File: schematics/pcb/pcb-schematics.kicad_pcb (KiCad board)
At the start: 2 copper layers, 145 x 77 mm, 0 parts

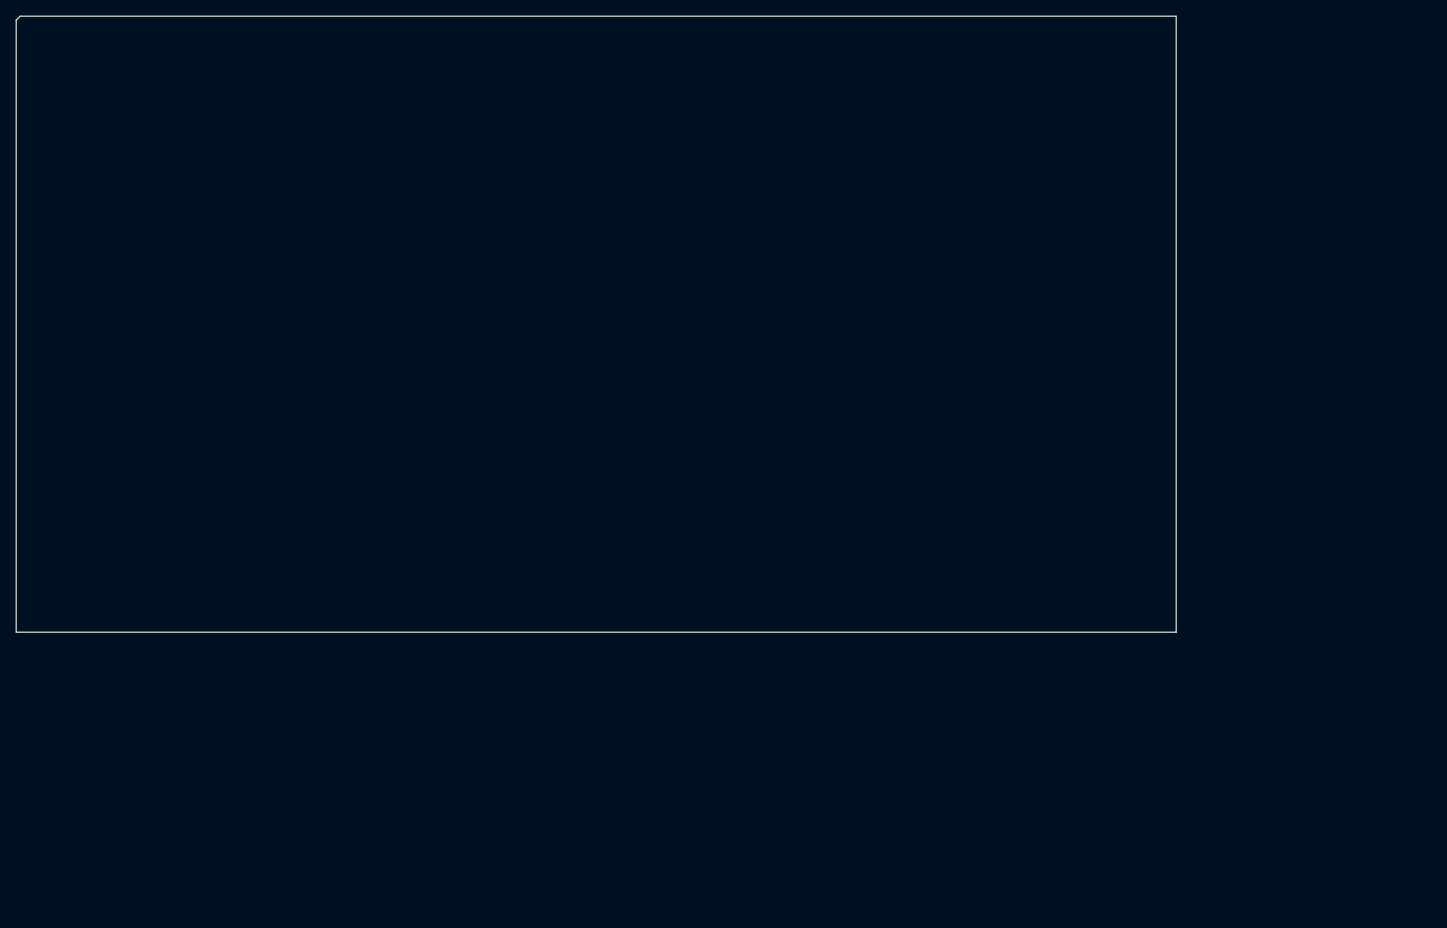
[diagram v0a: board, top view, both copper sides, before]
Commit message: schematic and driver rewrite
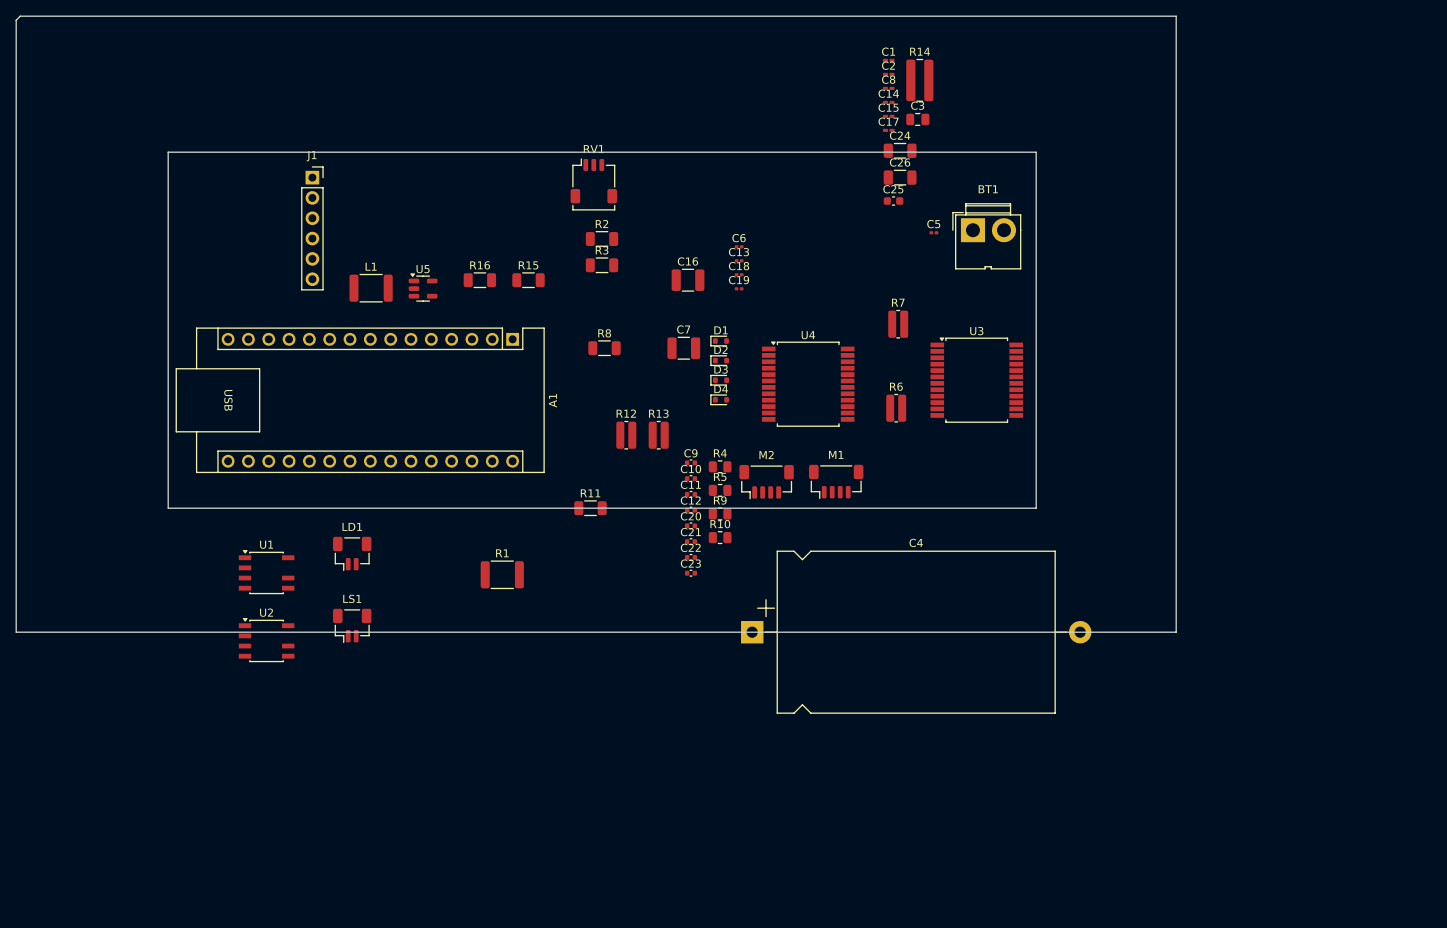
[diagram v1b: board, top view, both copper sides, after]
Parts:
- added A1: Arduino_Nano_33_BLE, Module:Arduino_Nano, F.Cu at (117.5, 88.4)
- added BT1: 9V, Connector:JWT_A3963_1x02_P3.96mm_Vertical, F.Cu at (175.1, 74.8)
- added C1: 10uF, Capacitor_SMD:C_0201_0603Metric_Pad0.64x0.40mm_HandSolder, F.Cu at (164.6, 53.5)
- added C10: 1000pF, Capacitor_SMD:C_0402_1005Metric, F.Cu at (139.9, 105.8)
- added C11: 1000pF, Capacitor_SMD:C_0402_1005Metric, F.Cu at (139.9, 107.8)
- added C12: 0.068uF, Capacitor_SMD:C_0402_1005Metric, F.Cu at (139.9, 109.7)
- added C13: 0.1uF, Capacitor_SMD:C_0201_0603Metric, F.Cu at (145.9, 78.6)
- added C14: 10uF, Capacitor_SMD:C_0201_0603Metric_Pad0.64x0.40mm_HandSolder, F.Cu at (164.6, 58.8)
- added C15: 0.1uF, Capacitor_SMD:C_0201_0603Metric_Pad0.64x0.40mm_HandSolder, F.Cu at (164.6, 60.5)
- added C16: 100uF, Capacitor_SMD:C_1210_3225Metric, F.Cu at (139.5, 81.0)
- added C17: 0.1uF, Capacitor_SMD:C_0201_0603Metric_Pad0.64x0.40mm_HandSolder, F.Cu at (164.6, 62.3)
- added C18: 0.01uF, Capacitor_SMD:C_0201_0603Metric, F.Cu at (145.9, 80.3)
- added C19: 0.22uF, Capacitor_SMD:C_0201_0603Metric, F.Cu at (145.9, 82.1)
- added C2: 10uF, Capacitor_SMD:C_0201_0603Metric_Pad0.64x0.40mm_HandSolder, F.Cu at (164.6, 55.3)
- added C20: 0.068uF, Capacitor_SMD:C_0402_1005Metric, F.Cu at (139.9, 111.7)
- added C21: 5600pF, Capacitor_SMD:C_0402_1005Metric, F.Cu at (139.9, 113.7)
- added C22: 1000pF, Capacitor_SMD:C_0402_1005Metric, F.Cu at (139.9, 115.7)
- added C23: 1000pF, Capacitor_SMD:C_0402_1005Metric, F.Cu at (139.9, 117.6)
- added C24: 22uF, Capacitor_SMD:C_1206_3216Metric, F.Cu at (166.0, 64.8)
- added C25: 4.7uF, Capacitor_SMD:C_0603_1608Metric, F.Cu at (165.2, 71.1)
- added C26: 22uF, Capacitor_SMD:C_1206_3216Metric, F.Cu at (166.0, 68.2)
- added C3: 0.05uF, Capacitor_SMD:C_0805_2012Metric, F.Cu at (168.2, 60.9)
- added C4: 250uF, Capacitor_THT:CP_Axial_L34.5mm_D20.0mm_P41.00mm_Horizontal, F.Cu at (147.5, 125.0)
- added C5: 0.01uF, Capacitor_SMD:C_0201_0603Metric, F.Cu at (170.2, 75.1)
- added C6: 0.22uF, Capacitor_SMD:C_0201_0603Metric, F.Cu at (145.9, 76.8)
- added C7: 100uF, Capacitor_SMD:C_1210_3225Metric, F.Cu at (139.0, 89.5)
- added C8: 0.1uF, Capacitor_SMD:C_0201_0603Metric_Pad0.64x0.40mm_HandSolder, F.Cu at (164.6, 57.0)
- added C9: 5600pF, Capacitor_SMD:C_0402_1005Metric, F.Cu at (139.9, 103.8)
- added D1: 1N4148, Diode_SMD:D_SOD-523, F.Cu at (143.6, 88.6)
- added D2: 1N4148, Diode_SMD:D_SOD-523, F.Cu at (143.6, 91.1)
- added D3: 1N4148, Diode_SMD:D_SOD-523, F.Cu at (143.6, 93.5)
- added D4: 1N4148, Diode_SMD:D_SOD-523, F.Cu at (143.6, 96.0)
- added J1: Micro_SD_Card, Connector_PinSocket_2.54mm:PinSocket_1x06_P2.54mm_Vertical, F.Cu at (92.5, 68.2)
- added L1: 2.2uH, Inductor_SMD:L_1812_4532Metric, F.Cu at (99.9, 82.0)
- added LD1: D_Laser_1C2A, Connector_Molex:Molex_Pico-Clasp_501331-0207_1x02-1MP_P1.00mm_Vertical, F.Cu at (97.5, 115.2)
- added LS1: Speaker, Connector_Molex:Molex_Pico-Clasp_501331-0207_1x02-1MP_P1.00mm_Vertical, F.Cu at (97.5, 124.2)
- added M1: Stepper_Motor_bipolar, Connector_Molex:Molex_Pico-Clasp_501331-0407_1x04-1MP_P1.00mm_Vertical, F.Cu at (158.0, 106.2)
- added M2: Stepper_Motor_bipolar, Connector_Molex:Molex_Pico-Clasp_501331-0407_1x04-1MP_P1.00mm_Vertical, F.Cu at (149.3, 106.2)
- added R1: 10, Resistor_SMD:R_1812_4532Metric, F.Cu at (116.3, 117.8)
- added R10: 0.3, Resistor_SMD:R_0805_2012Metric, F.Cu at (143.5, 113.2)
- added R11: 100K, Resistor_SMD:R_1206_3216Metric, F.Cu at (127.3, 109.5)
- added R12: 39K, Resistor_SMD:R_0612_1632Metric, F.Cu at (131.8, 100.4)
- added R13: 39K, Resistor_SMD:R_0612_1632Metric, F.Cu at (135.8, 100.4)
- added R14: 1K, Resistor_SMD:R_1020_2550Metric, F.Cu at (168.4, 56.0)
- added R15: 200K, Resistor_SMD:R_1206_3216Metric, F.Cu at (119.5, 81.0)
- added R16: 100K, Resistor_SMD:R_1206_3216Metric, F.Cu at (113.5, 81.0)
- added R2: 100, Resistor_SMD:R_1206_3216Metric, F.Cu at (128.7, 75.8)
- added R3: 100K, Resistor_SMD:R_1206_3216Metric, F.Cu at (128.7, 79.1)
- added R4: 0.3, Resistor_SMD:R_0805_2012Metric, F.Cu at (143.5, 104.3)
- added R5: 0.3, Resistor_SMD:R_0805_2012Metric, F.Cu at (143.5, 107.3)
- added R6: 39K, Resistor_SMD:R_0612_1632Metric, F.Cu at (165.5, 97.0)
- added R7: 39K, Resistor_SMD:R_0612_1632Metric, F.Cu at (165.8, 86.5)
- added R8: 100, Resistor_SMD:R_1206_3216Metric, F.Cu at (129.0, 89.5)
- added R9: 0.3, Resistor_SMD:R_0805_2012Metric, F.Cu at (143.5, 110.2)
- added RV1: 10K, Connector_Molex:Molex_Pico-Clasp_202396-0307_1x03-1MP_P1.00mm_Horizontal, F.Cu at (127.7, 68.6)
- added U1: LM386, Package_SO:SOIC-8-N7_3.9x4.9mm_P1.27mm, F.Cu at (86.8, 117.6)
- added U2: MCP4901, Package_SO:SOIC-8-N7_3.9x4.9mm_P1.27mm, F.Cu at (86.8, 126.1)
- added U3: L6208D, Package_SO:ST_PowerSSO-24_SlugUp, F.Cu at (175.6, 93.5)
- added U4: L6208D, Package_SO:ST_PowerSSO-24_SlugUp, F.Cu at (154.5, 94.0)
- added U5: TLV62568DBV, Package_TO_SOT_SMD:SOT-23-5, F.Cu at (106.4, 82.0)
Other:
- outline, holes or cut-outs redrawn

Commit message: KiCad schematics at manufacture
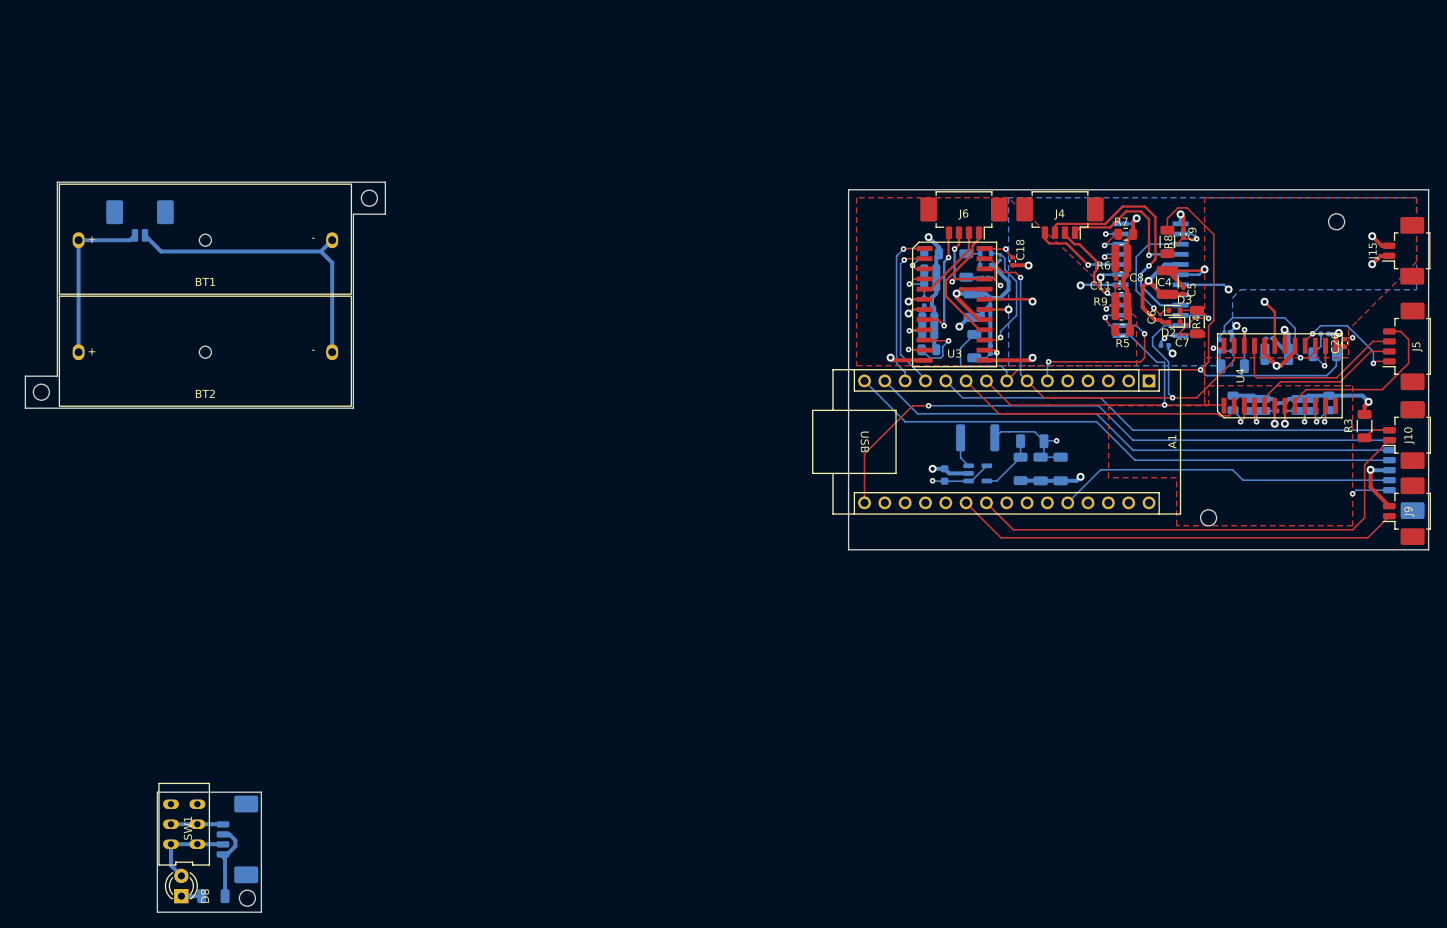
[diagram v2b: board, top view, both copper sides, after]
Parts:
- removed D1: 1N4148, Diode_SMD:D_SOD-523
- removed J1: Micro_SD_Card, Connector_PinSocket_2.54mm:PinSocket_1x06_P2.54mm_Vertical
- removed LD1: D_Laser_1C2A, Connector_Molex:Molex_Pico-Clasp_501331-0207_1x02-1MP_P1.00mm_Vertical
- removed LS1: Speaker, Connector_Molex:Molex_Pico-Clasp_501331-0207_1x02-1MP_P1.00mm_Vertical
- removed M1, M2: Stepper_Motor_bipolar, Connector_Molex:Molex_Pico-Clasp_501331-0407_1x04-1MP_P1.00mm_Vertical
- removed RV1: 10K, Connector_Molex:Molex_Pico-Clasp_202396-0307_1x03-1MP_P1.00mm_Horizontal
- removed U5: TLV62568DBV, Package_TO_SOT_SMD:SOT-23-5
- added BT2: Battery, PersonalLibraries:Battery_clip-MPD_BHA23APC, F.Cu at (79.2, 90.0)
- added C27: 1000pF, Capacitor_SMD:C_0402_1005Metric, B.Cu at (213.1, 96.9)
- added D5: 1N4148, Diode_SMD:D_SOD-523, B.Cu at (176.7, 77.7)
- added D6: 1N4148, Diode_SMD:D_SOD-523, B.Cu at (207.5, 89.1)
- added D7: 1N4148, Diode_SMD:D_SOD-523, B.Cu at (206.0, 89.1)
- added D8: LED, LED_THT:LED_D3.0mm, F.Cu at (76.2, 158.0)
- added J10: Conn_01x02_Socket, Connector_Molex:Molex_PicoBlade_53261-0271_1x02-1MP_P1.25mm_Horizontal, F.Cu at (229.6, 100.4)
- added J11: Conn_01x07_Socket, Connector_Molex:Molex_PicoBlade_53261-0771_1x07-1MP_P1.25mm_Horizontal, B.Cu at (229.6, 103.5)
- added J15: Conn_01x02_Socket, Connector_Molex:Molex_PicoBlade_53261-0271_1x02-1MP_P1.25mm_Horizontal, F.Cu at (229.5, 77.3)
- added J4: Conn_01x04_Socket, Connector_Molex:Molex_PicoBlade_53261-0471_1x04-1MP_P1.25mm_Horizontal, F.Cu at (186.0, 72.7)
- added J5: Conn_01x04_Socket, Connector_Molex:Molex_PicoBlade_53261-0471_1x04-1MP_P1.25mm_Horizontal, F.Cu at (229.6, 89.3)
- added J6: Conn_01x04_Socket, Connector_Molex:Molex_PicoBlade_53261-0471_1x04-1MP_P1.25mm_Horizontal, F.Cu at (174.0, 72.7)
- added J7: Conn_01x04_Socket, Connector_Molex:Molex_PicoBlade_53261-0471_1x04-1MP_P1.25mm_Horizontal, B.Cu at (83.8, 150.9)
- added J8: Conn_01x02_Socket, Connector_Molex:Molex_PicoBlade_53261-0271_1x02-1MP_P1.25mm_Horizontal, B.Cu at (71.0, 73.0)
- added J9: Conn_01x02_Socket, Connector_Molex:Molex_PicoBlade_53261-0271_1x02-1MP_P1.25mm_Horizontal, F.Cu at (229.6, 109.9)
- added R17: 0.3, Resistor_SMD:R_0805_2012Metric, B.Cu at (207.6, 96.3)
- added R18: 0.3, Resistor_SMD:R_0805_2012Metric, B.Cu at (219.6, 96.3)
- added R19: 39K, Resistor_SMD:R_0612_1632Metric, B.Cu at (216.6, 96.6)
- added R20: 100K, Resistor_SMD:R_1206_3216Metric, B.Cu at (219.1, 90.3)
- added R21: 39K, Resistor_SMD:R_0612_1632Metric, B.Cu at (210.6, 96.6)
- added R22: 100K, Resistor_SMD:R_1206_3216Metric, B.Cu at (80.2, 158.0)
- added SW1: SW_DPDT_x2, PersonalLibraries:SW-Slide_Diptronics-LSSA22, F.Cu at (76.5, 149.0)
- BT1: value 9V -> Battery; footprint Connector:JWT_A3963_1x02_P3.96mm_Vertical -> PersonalLibraries:Battery_clip-MPD_BHA23APC
- C1, C2: value 10uF -> 22uF; footprint Capacitor_SMD:C_0201_0603Metric_Pad0.64x0.40mm_HandSolder -> Capacitor_SMD:C_1206_3216Metric; moved to B.Cu
- C10: value 1000pF -> 0.068uF; moved to B.Cu
- C12, C20: value 0.068uF -> 100uF; footprint Capacitor_SMD:C_0402_1005Metric -> Capacitor_SMD:C_1210_3225Metric; moved to B.Cu
- C13: footprint Capacitor_SMD:C_0201_0603Metric -> Capacitor_SMD:C_0201_0603Metric_Pad0.64x0.40mm_HandSolder; moved to B.Cu
- C14: value 10uF -> 0.22uF; footprint Capacitor_SMD:C_0201_0603Metric_Pad0.64x0.40mm_HandSolder -> Capacitor_SMD:C_0201_0603Metric; moved to B.Cu
- C15: value 0.1uF -> 0.01uF; footprint Capacitor_SMD:C_0201_0603Metric_Pad0.64x0.40mm_HandSolder -> Capacitor_SMD:C_0201_0603Metric; moved to B.Cu
- C16: value 100uF -> 1000pF; footprint Capacitor_SMD:C_1210_3225Metric -> Capacitor_SMD:C_0402_1005Metric; moved to B.Cu
- C17: value 0.1uF -> 5600pF; footprint Capacitor_SMD:C_0201_0603Metric_Pad0.64x0.40mm_HandSolder -> Capacitor_SMD:C_0402_1005Metric; moved to B.Cu
- C18: value 0.01uF -> 0.068uF; footprint Capacitor_SMD:C_0201_0603Metric -> Capacitor_SMD:C_0402_1005Metric
- C19: value 0.22uF -> 1000pF; footprint Capacitor_SMD:C_0201_0603Metric -> Capacitor_SMD:C_0402_1005Metric; moved to B.Cu
- C21: value 5600pF -> 0.1uF; footprint Capacitor_SMD:C_0402_1005Metric -> Capacitor_SMD:C_0201_0603Metric_Pad0.64x0.40mm_HandSolder; moved to B.Cu
- C22: value 1000pF -> 0.22uF; footprint Capacitor_SMD:C_0402_1005Metric -> Capacitor_SMD:C_0201_0603Metric; moved to B.Cu
- C23: value 1000pF -> 0.01uF; footprint Capacitor_SMD:C_0402_1005Metric -> Capacitor_SMD:C_0201_0603Metric; moved to B.Cu
- C24: value 22uF -> 1000pF; footprint Capacitor_SMD:C_1206_3216Metric -> Capacitor_SMD:C_0402_1005Metric; moved to B.Cu
- C25: value 4.7uF -> 5600pF; footprint Capacitor_SMD:C_0603_1608Metric -> Capacitor_SMD:C_0402_1005Metric; moved to B.Cu
- C26: value 22uF -> 0.068uF; footprint Capacitor_SMD:C_1206_3216Metric -> Capacitor_SMD:C_0402_1005Metric
- C3: value 0.05uF -> 4.7uF; footprint Capacitor_SMD:C_0805_2012Metric -> Capacitor_SMD:C_0603_1608Metric; moved to B.Cu
- C4: value 250uF -> 100uF; footprint Capacitor_THT:CP_Axial_L34.5mm_D20.0mm_P41.00mm_Horizontal -> Capacitor_SMD:C_1210_3225Metric
- C5: value 0.01uF -> 0.1uF; footprint Capacitor_SMD:C_0201_0603Metric -> Capacitor_SMD:C_0201_0603Metric_Pad0.64x0.40mm_HandSolder
- C7: value 100uF -> 0.01uF; footprint Capacitor_SMD:C_1210_3225Metric -> Capacitor_SMD:C_0201_0603Metric
- C8: value 0.1uF -> 1000pF; footprint Capacitor_SMD:C_0201_0603Metric_Pad0.64x0.40mm_HandSolder -> Capacitor_SMD:C_0402_1005Metric
- D4, L1, R13: moved to B.Cu
- R1: value 10 -> 100K; footprint Resistor_SMD:R_1812_4532Metric -> Resistor_SMD:R_1206_3216Metric; moved to B.Cu
- R10: value 0.3 -> 100; footprint Resistor_SMD:R_0805_2012Metric -> Resistor_SMD:R_1206_3216Metric; moved to B.Cu
- R11: value 100K -> 0.3; footprint Resistor_SMD:R_1206_3216Metric -> Resistor_SMD:R_0805_2012Metric; moved to B.Cu
- R12: value 39K -> 0.3; footprint Resistor_SMD:R_0612_1632Metric -> Resistor_SMD:R_0805_2012Metric; moved to B.Cu
- R14: value 1K -> 100K; footprint Resistor_SMD:R_1020_2550Metric -> Resistor_SMD:R_1206_3216Metric; moved to B.Cu
- R15: value 200K -> 39K; footprint Resistor_SMD:R_1206_3216Metric -> Resistor_SMD:R_0612_1632Metric; moved to B.Cu
- R16: value 100K -> 100; moved to B.Cu
- R2: value 100 -> 200K; moved to B.Cu
- R3: value 100K -> 100
- R4: value 0.3 -> 100; footprint Resistor_SMD:R_0805_2012Metric -> Resistor_SMD:R_1206_3216Metric
- R6: value 39K -> 0.3; footprint Resistor_SMD:R_0612_1632Metric -> Resistor_SMD:R_0805_2012Metric
- R8: value 100 -> 100K
- R9: value 0.3 -> 39K; footprint Resistor_SMD:R_0805_2012Metric -> Resistor_SMD:R_0612_1632Metric
- U1: value LM386 -> TLV62568DBV; footprint Package_SO:SOIC-8-N7_3.9x4.9mm_P1.27mm -> Package_TO_SOT_SMD:SOT-23-5; moved to B.Cu
- U2: value MCP4901 -> L6208D; footprint Package_SO:SOIC-8-N7_3.9x4.9mm_P1.27mm -> Package_SO:SO24_7.5x15.3mm_P1.27mm; moved to B.Cu
- U3, U4: footprint Package_SO:ST_PowerSSO-24_SlugUp -> Package_SO:SO24_7.5x15.3mm_P1.27mm
- moved U2 119.4 mm to (197.3, 80.9), turned to 90 degrees
- moved R3 97.4 mm to (224.1, 99.2), turned to 90 degrees
- moved BT1 96.0 mm to (79.2, 76.0)
- moved R16 94.7 mm to (207.6, 91.8)
- moved U1 89.8 mm to (175.7, 105.2)
- moved A1 79.7 mm to (197.1, 93.6)
- moved L1 78.1 mm to (175.7, 100.7), turned to 180 degrees
- moved C21 76.6 mm to (212.1, 88.3), turned to 180 degrees
- moved C20 76.3 mm to (213.1, 90.3), turned to 180 degrees
- moved C23 74.6 mm to (209.0, 89.6), turned to 90 degrees
- moved C22 72.7 mm to (206.8, 87.4), turned to 180 degrees
- moved R8 71.6 mm to (199.4, 76.2), turned to 90 degrees
- moved R1 68.3 mm to (182.5, 101.1)
- moved C9 67.9 mm to (201.4, 75.2), turned to -90 degrees
- moved C4 67.9 mm to (199.4, 81.3), turned to -90 degrees
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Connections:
- A1 pad 1: Net-(A1-D1/TX) -> unconnected-(A1-D0/TX-Pad1)
- A1 pad 10: unconnected-(A1-D7-Pad10) -> /Motor Driver2/CW/CCW
- A1 pad 12: Net-(A1-D9) -> /Motor Driver1/CW/CCW
- A1 pad 13: Net-(A1-D10) -> /Motor Driver1/CLK
- A1 pad 14: Net-(A1-D11) -> Net-(A1-D11/MOSI)
- A1 pad 16: Net-(A1-D13) -> Net-(A1-D13/CLK)
- A1 pad 2: Net-(A1-D0/RX) -> unconnected-(A1-D1/RX-Pad2)
- A1 pad 21: unconnected-(A1-A2-Pad21) -> Net-(A1-A2)
- A1 pad 22: unconnected-(A1-A3-Pad22) -> Net-(A1-A3)
- A1 pad 26: unconnected-(A1-A7-Pad26) -> Net-(A1-A7)
- A1 pad 27: Net-(A1-+5V) -> unconnected-(A1-+5V-Pad27)
- A1 pad 29: Net-(BT1--) -> GND
- A1 pad 30: Net-(A1-VIN) -> +12V
- A1 pad 4: Net-(BT1--) -> GND
- A1 pad 5: Net-(A1-D2) -> unconnected-(A1-D2-Pad5)
- A1 pad 6: Net-(A1-D3) -> /Motor Driver/CW/CCW
- A1 pad 7: unconnected-(A1-D4-Pad7) -> /Motor Driver/RESET
- A1 pad 8: unconnected-(A1-D5-Pad8) -> /Motor Driver/EN
- A1 pad 9: unconnected-(A1-D6-Pad9) -> /Motor Driver/CLK
- BT1 pad 1: Net-(A1-VIN) -> Net-(BT1-+)
- C1 pad 1: Net-(C1-Pad1) -> GND
- C1 pad 2: Net-(C1-Pad2) -> /Motor Driver/VREF
- C10 pad 1: Net-(U3-RCB) -> GND
- C10 pad 2: Net-(BT1--) -> /Motor Driver/VREF
- C11 pad 1: Net-(U3-RCA) -> Net-(U2-RCA)
- C11 pad 2: Net-(BT1--) -> GND
- C12 pad 1: Net-(C12-Pad1) -> GND
- C12 pad 2: Net-(U3-VREFA) -> +12V
- C13 pad 1: Net-(A1-3V3) -> GND
- C13 pad 2: Net-(BT1--) -> +12V
- C14 pad 1: Net-(A1-3V3) -> +12V
- C14 pad 2: Net-(BT1--) -> Net-(D5-K)
- C15 pad 1: Net-(A1-3V3) -> Net-(C15-Pad1)
- C15 pad 2: Net-(BT1--) -> Net-(U3-VCP)
- C16 pad 1: Net-(BT1--) -> Net-(U3-RCB)
- C16 pad 2: Net-(A1-VIN) -> GND
- C17 pad 1: Net-(A1-VIN) -> GND
- C17 pad 2: Net-(BT1--) -> Net-(U3-EN)
- C18 pad 1: Net-(C18-Pad1) -> GND
- C18 pad 2: Net-(U4-VCP) -> /Motor Driver/VREF
- C19 pad 1: Net-(A1-VIN) -> Net-(U3-RCA)
- C19 pad 2: Net-(D4-K) -> GND
- C2 pad 1: Net-(U2-Vout) -> GND
- C2 pad 2: Net-(C2-Pad2) -> /Motor Driver/VREF
- C20 pad 1: Net-(C12-Pad1) -> GND
- C20 pad 2: Net-(U4-VREFA) -> +12V
- C21 pad 1: Net-(U4-EN) -> GND
- C21 pad 2: Net-(BT1--) -> +12V
- C22 pad 1: Net-(U4-RCA) -> +12V
- C22 pad 2: Net-(BT1--) -> Net-(D7-K)
- C23 pad 1: Net-(U4-RCB) -> Net-(C23-Pad1)
- C23 pad 2: Net-(BT1--) -> Net-(U4-VCP)
- C24 pad 1: Net-(BT1--) -> Net-(U4-RCB)
- C24 pad 2: Net-(C12-Pad1) -> GND
- C25 pad 1: Net-(A1-3V3) -> GND
- C25 pad 2: Net-(BT1--) -> Net-(U4-EN)
- C26 pad 1: Net-(BT1--) -> GND
- C26 pad 2: Net-(C12-Pad1) -> /Motor Driver/VREF
- C3 pad 1: Net-(C3-Pad1) -> Net-(A1-3V3)
- C3 pad 2: Net-(C3-Pad2) -> GND
- C4 pad 1: Net-(C3-Pad1) -> GND
- C4 pad 2: Net-(C4-Pad2) -> +12V
- C5 pad 1: Net-(C5-Pad1) -> GND
- C5 pad 2: Net-(U3-VCP) -> +12V
- C6 pad 1: Net-(A1-VIN) -> +12V
- C6 pad 2: Net-(D2-K) -> Net-(D3-K)
- C7 pad 1: Net-(BT1--) -> Net-(C7-Pad1)
- C7 pad 2: Net-(A1-VIN) -> Net-(U2-VCP)
- C8 pad 1: Net-(BT1--) -> Net-(U2-RCB)
- C8 pad 2: Net-(A1-VIN) -> GND
- C9 pad 1: Net-(U3-EN) -> GND
- C9 pad 2: Net-(BT1--) -> Net-(U2-EN)
- D2 pad 2: Net-(D1-K) -> +12V
- D3 pad 2: Net-(A1-VIN) -> Net-(D2-K)
- D4 pad 2: Net-(D3-K) -> +12V
- L1 pad 1: Net-(C12-Pad1) -> /Motor Driver/VREF
- L1 pad 2: Net-(U5-SW) -> Net-(U1-SW)
- R1 pad 1: Net-(C3-Pad2) -> Net-(U1-FB)
- R1 pad 2: Net-(BT1--) -> /Motor Driver/VREF
- R10 pad 1: Net-(BT1--) -> Net-(D4-K)
- R10 pad 2: Net-(U4-SENSE_B) -> Net-(C15-Pad1)
- R11 pad 1: Net-(U4-EN) -> GND
- R11 pad 2: Net-(A1-D0/RX) -> Net-(U3-SENSE_A)
- R12 pad 1: Net-(U4-RCA) -> GND
- R12 pad 2: Net-(BT1--) -> Net-(U3-SENSE_B)
- R13 pad 1: Net-(U4-RCB) -> Net-(U3-RCB)
- R13 pad 2: Net-(BT1--) -> GND
- R14 pad 1: Net-(A1-3V3) -> Net-(U3-EN)
- R14 pad 2: Net-(A1-D10) -> /Motor Driver/EN
- R15 pad 1: Net-(BT1--) -> Net-(U3-RCA)
- R15 pad 2: Net-(C12-Pad1) -> GND
- R16 pad 2: Net-(C12-Pad1) -> Net-(C23-Pad1)
- R2 pad 1: Net-(D1-K) -> GND
- R2 pad 2: Net-(C5-Pad1) -> Net-(U1-FB)
- R3 pad 1: Net-(U3-EN) -> Net-(J10-Pin_2)
- R3 pad 2: Net-(A1-D0/RX) -> GND
- R4 pad 1: Net-(BT1--) -> Net-(D2-K)
- R4 pad 2: Net-(U3-SENSE_A) -> Net-(C7-Pad1)
- R5 pad 1: Net-(BT1--) -> GND
- R5 pad 2: Net-(U3-SENSE_B) -> Net-(U2-SENSE_A)
- R6 pad 1: Net-(U3-RCB) -> GND
- R6 pad 2: Net-(BT1--) -> Net-(U2-SENSE_B)
- R7 pad 1: Net-(U3-RCA) -> Net-(U2-RCB)
- R7 pad 2: Net-(BT1--) -> GND
- R8 pad 1: Net-(D3-K) -> Net-(U2-EN)
- R8 pad 2: Net-(C18-Pad1) -> /Motor Driver/EN
- R9 pad 1: Net-(BT1--) -> Net-(U2-RCA)
- R9 pad 2: Net-(U4-SENSE_A) -> GND
- U1 pad 1: Net-(C1-Pad2) -> Net-(A1-3V3)
- U1 pad 2: Net-(BT1--) -> GND
- U1 pad 3: Net-(U1-+) -> Net-(U1-SW)
- U1 pad 4: Net-(BT1--) -> Net-(A1-3V3)
- U1 pad 5: Net-(C3-Pad1) -> Net-(U1-FB)
- U2 pad 1: Net-(A1-3V3) -> /Motor Driver/CLK
- U2 pad 2: Net-(A1-D9) -> /Motor Driver/CW/CCW
- U2 pad 3: Net-(A1-D13) -> Net-(U2-SENSE_A)
- U2 pad 4: Net-(A1-D11) -> Net-(U2-RCA)
- U2 pad 5: Net-(BT1--) -> /Motor Driver/OUT1A
- U2 pad 6: Net-(A1-3V3) -> GND
- U2 pad 8: Net-(U2-Vout) -> /Motor Driver/OUT1B
- U3 pad 1: Net-(A1-D1/TX) -> /Motor Driver1/CLK
- U3 pad 11: Net-(U3-VREFA) -> /Motor Driver/VREF
- U3 pad 12: Net-(BT1--) -> GND
- U3 pad 13: Net-(BT1--) -> GND
- U3 pad 15: Net-(D2-K) -> Net-(D5-K)
- U3 pad 16: Net-(U3-OUT2B) -> /Motor Driver1/OUT2B
- U3 pad 17: Net-(A1-VIN) -> +12V
- U3 pad 18: Net-(BT1--) -> GND
- U3 pad 19: Net-(BT1--) -> GND
- U3 pad 2: Net-(A1-D2) -> /Motor Driver1/CW/CCW
- U3 pad 20: Net-(A1-VIN) -> +12V
- U3 pad 21: Net-(M1--) -> /Motor Driver1/OUT2A
- U3 pad 23: Net-(A1-+5V) -> /Motor Driver/RESET
- U3 pad 24: Net-(U3-VREFA) -> /Motor Driver/VREF
- U3 pad 5: Net-(U3-OUT1A) -> /Motor Driver1/OUT1A
- U3 pad 6: Net-(BT1--) -> GND
- U3 pad 7: Net-(BT1--) -> GND
- U3 pad 8: Net-(U3-OUT1B) -> /Motor Driver1/OUT1B
- U4 pad 1: Net-(A1-D1/TX) -> /Motor Driver/CLK
- U4 pad 11: Net-(U4-VREFA) -> /Motor Driver/VREF
- U4 pad 12: Net-(BT1--) -> GND
- U4 pad 13: Net-(BT1--) -> GND
- U4 pad 15: Net-(D4-K) -> Net-(D7-K)
- U4 pad 16: Net-(U4-OUT2B) -> /Motor Driver2/OUT2B
- U4 pad 17: Net-(A1-VIN) -> +12V
- U4 pad 18: Net-(BT1--) -> GND
- U4 pad 19: Net-(BT1--) -> GND
- U4 pad 2: Net-(A1-D3) -> /Motor Driver2/CW/CCW
- U4 pad 20: Net-(A1-VIN) -> +12V
- U4 pad 21: Net-(M2--) -> /Motor Driver2/OUT2A
- U4 pad 23: Net-(A1-+5V) -> /Motor Driver/RESET
- U4 pad 24: Net-(U4-VREFA) -> /Motor Driver/VREF
- U4 pad 5: Net-(U4-OUT1A) -> /Motor Driver2/OUT1A
- U4 pad 6: Net-(BT1--) -> GND
- U4 pad 7: Net-(BT1--) -> GND
- U4 pad 8: Net-(U4-OUT1B) -> /Motor Driver2/OUT1B
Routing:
- net GND: track 0.00 -> 166.3 mm, vias 0 -> 26
- net /Motor Driver/VREF: track 0.00 -> 149.2 mm, vias 0 -> 8
- net /Motor Driver/EN: track 0.00 -> 82.7 mm, vias 0 -> 1
- net Net-(A1-D13/CLK): track 0.00 -> 76.0 mm, vias 0 -> 1
- net Net-(A1-3V3): track 0.00 -> 75.0 mm, vias 0 -> 2
- net Net-(A1-D12/MISO): track 0.00 -> 69.8 mm
- net Net-(A1-D11/MOSI): track 0.00 -> 66.7 mm
- net /Motor Driver/RESET: track 0.00 -> 61.9 mm, vias 0 -> 2
- net Net-(A1-A3): track 0.00 -> 60.3 mm
- net +12V: track 0.00 -> 59.6 mm, vias 0 -> 5
- net Net-(A1-D8): track 0.00 -> 58.0 mm
- net Net-(A1-A2): track 0.00 -> 55.8 mm
- net /Motor Driver/CLK: track 0.00 -> 43.2 mm, vias 0 -> 1
- net Net-(A1-A7): track 0.00 -> 42.5 mm
- net Net-(BT1--): track 0.00 -> 38.0 mm
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- added copper zone on In2.Cu, net +12V
- added copper zone on B.Cu, net GND
- added copper zone on F.Cu, net GND
- added copper zone on In1.Cu, net GND
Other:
- board size 145 x 77 mm -> 175.4 x 91.2 mm
- copper layers 2 -> 4
